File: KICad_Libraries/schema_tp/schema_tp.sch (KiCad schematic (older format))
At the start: 2 parts, among them U1 Touchpad_mp

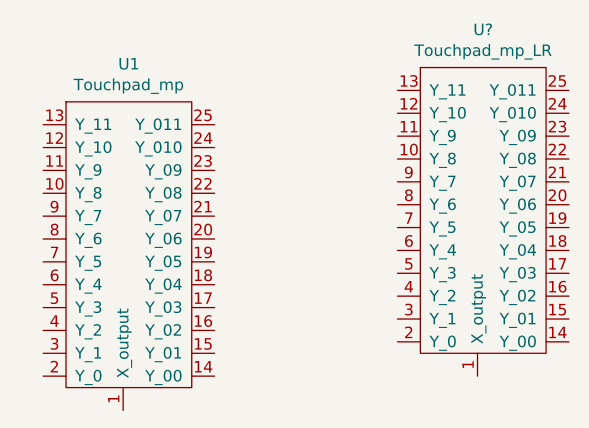
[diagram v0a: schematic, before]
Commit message: update 23/03/2021 alle libraries aangepast naar definitieve componenten
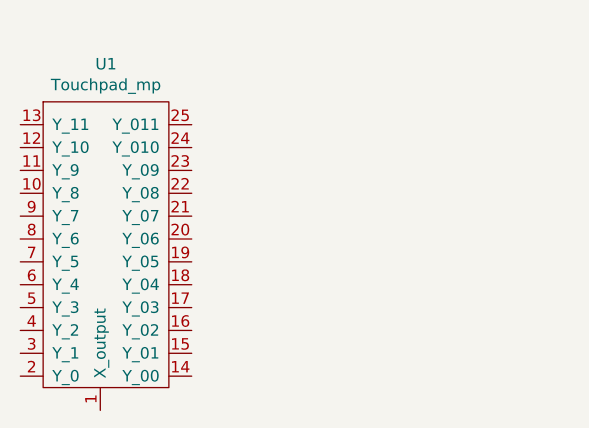
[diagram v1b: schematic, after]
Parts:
- removed U?: Touchpad_mp_LR, symbol touchpad_lib:Touchpad_mp_LR
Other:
- moved on the sheet: U1
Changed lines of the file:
@@
 L touchpad_lib:Touchpad_mp U1
 U 1 1 603E343B
-P 3500 3100
-F 0 "U1" H 3575 3465 50  0000 C CNN
-F 1 "Touchpad_mp" H 3575 3374 50  0000 C CNN
-F 2 "mengpaneel:touchpad_footprint" H 3500 3600 50  0001 C CNN
-F 3 "" H 3500 3600 50  0001 C CNN
-	1    3500 3100
+P 3400 3100
+F 0 "U1" H 3475 3465 50  0000 C CNN
+F 1 "Touchpad_mp" H 3475 3374 50  0000 C CNN
+F 2 "mengpaneel:touchpad_footprint" H 3400 3600 50  0001 C CNN
+F 3 "" H 3400 3600 50  0001 C CNN
+	1    3400 3100
 	1    0    0    -1
 $EndComp
-$Comp
-L touchpad_lib:Touchpad_mp_LR U?
-U 1 1 60509689
-P 5050 2950
-F 0 "U?" H 5125 3315 50  0000 C CNN
-F 1 "Touchpad_mp_LR" H 5125 3224 50  0000 C CNN
-F 2 "" H 5050 3450 50  0001 C CNN
-F 3 "" H 5050 3450 50  0001 C CNN
-	1    5050 2950
-	1    0    0    -1
-$EndComp

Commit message: Footprints sliders aangepast + slider links-rechts footprint toegevoegd
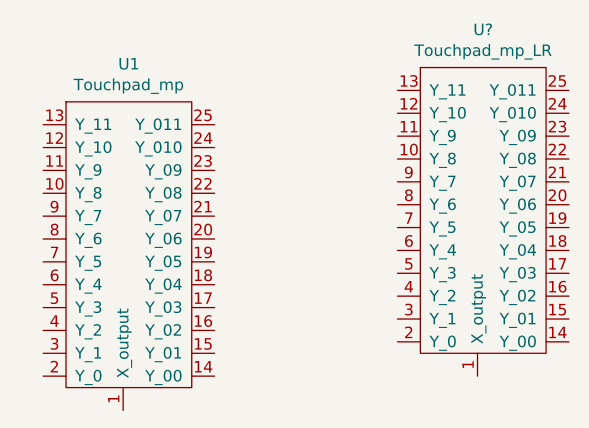
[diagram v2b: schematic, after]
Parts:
- added U?: Touchpad_mp_LR, symbol touchpad_lib:Touchpad_mp_LR
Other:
- moved on the sheet: U1
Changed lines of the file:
@@
 L touchpad_lib:Touchpad_mp U1
 U 1 1 603E343B
-P 3400 3100
-F 0 "U1" H 3475 3465 50  0000 C CNN
-F 1 "Touchpad_mp" H 3475 3374 50  0000 C CNN
-F 2 "mengpaneel:touchpad_footprint" H 3400 3600 50  0001 C CNN
-F 3 "" H 3400 3600 50  0001 C CNN
-	1    3400 3100
+P 3500 3100
+F 0 "U1" H 3575 3465 50  0000 C CNN
+F 1 "Touchpad_mp" H 3575 3374 50  0000 C CNN
+F 2 "mengpaneel:touchpad_footprint" H 3500 3600 50  0001 C CNN
+F 3 "" H 3500 3600 50  0001 C CNN
+	1    3500 3100
 	1    0    0    -1
 $EndComp
+$Comp
+L touchpad_lib:Touchpad_mp_LR U?
+U 1 1 60509689
+P 5050 2950
+F 0 "U?" H 5125 3315 50  0000 C CNN
+F 1 "Touchpad_mp_LR" H 5125 3224 50  0000 C CNN
+F 2 "" H 5050 3450 50  0001 C CNN
+F 3 "" H 5050 3450 50  0001 C CNN
+	1    5050 2950
+	1    0    0    -1
+$EndComp
